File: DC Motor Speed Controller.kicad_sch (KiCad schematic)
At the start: 15 parts, among them J1 Screw_Terminal_01x02, J2 Screw_Terminal_01x02, Q1 TIP122, U1 NE555P

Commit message: Assigned Footprints to Components
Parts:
- C1, C2: footprint (none) -> Capacitor_THT:C_Disc_D4.7mm_W2.5mm_P5.00mm
- C3: footprint (none) -> Capacitor_THT:CP_Radial_D10.0mm_P5.00mm
- D4: footprint (none) -> LED_THT:LED_D5.0mm
- J1, J2: footprint (none) -> TerminalBlock:TerminalBlock_bornier-2_P5.08mm
- R1, R2, R3: footprint (none) -> Resistor_THT:R_Axial_DIN0204_L3.6mm_D1.6mm_P7.62mm_Horizontal
- RV1: footprint (none) -> Potentiometer_THT:Potentiometer_Alps_RK097_Single_Horizontal_Switch
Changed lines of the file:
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@@
 			)
 		)
-		(property "Footprint" ""
+		(property "Footprint" "Potentiometer_THT:Potentiometer_Alps_RK097_Single_Horizontal_Switch"
 			(at 90.17 100.33 0)
 			(effects
@@
 			)
 		)
-		(property "Footprint" ""
+		(property "Footprint" "LED_THT:LED_D5.0mm"
 			(at 72.39 113.03 0)
 			(effects
@@
 			)
 		)
-		(property "Footprint" ""
+		(property "Footprint" "Capacitor_THT:CP_Radial_D10.0mm_P5.00mm"
 			(at 63.1952 104.14 0)
 			(effects
@@
 			)
 		)
-		(property "Footprint" ""
+		(property "Footprint" "Resistor_THT:R_Axial_DIN0204_L3.6mm_D1.6mm_P7.62mm_Horizontal"
 			(at 171.45 91.948 90)
 			(effects
@@
 			)
 		)
-		(property "Footprint" ""
+		(property "Footprint" "Capacitor_THT:C_Disc_D4.7mm_W2.5mm_P5.00mm"
 			(at 91.1352 118.11 0)
 			(effects
@@
 			)
 		)
-		(property "Footprint" ""
+		(property "Footprint" "Capacitor_THT:C_Disc_D4.7mm_W2.5mm_P5.00mm"
 			(at 119.0752 118.11 0)
 			(effects
@@
 			)
 		)
-		(property "Footprint" ""
+		(property "Footprint" "Resistor_THT:R_Axial_DIN0204_L3.6mm_D1.6mm_P7.62mm_Horizontal"
 			(at 88.392 73.66 90)
 			(effects
@@
 			)
 		)
-		(property "Footprint" ""
+		(property "Footprint" "TerminalBlock:TerminalBlock_bornier-2_P5.08mm"
 			(at 210.82 74.93 0)
 			(effects
@@
 			)
 		)
-		(property "Footprint" ""
+		(property "Footprint" "Resistor_THT:R_Axial_DIN0204_L3.6mm_D1.6mm_P7.62mm_Horizontal"
 			(at 70.612 73.66 90)
 			(effects
@@
 			)
 		)
-		(property "Footprint" ""
+		(property "Footprint" "TerminalBlock:TerminalBlock_bornier-2_P5.08mm"
 			(at 46.99 97.79 0)
 			(effects

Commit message: Assigned the Error footprint
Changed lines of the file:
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@@
-	)
-	(symbol
-		(lib_id "Device:C")
-		(at 62.23 100.33 0)
-		(unit 1)
-		(exclude_from_sim no)
-		(in_bom yes)
-		(on_board yes)
-		(dnp no)
-		(property "Reference" "C3"
-			(at 66.04 99.0599 0)
-			(effects
-				(font
-					(size 1.27 1.27)
-				)
-				(justify left)
-			)
-		)
-		(property "Value" "1000uF"
-			(at 63.754 109.22 90)
-			(effects
-				(font
-					(size 1.27 1.27)
-				)
-				(justify left)
-			)
-		)
-		(property "Footprint" "Capacitor_THT:CP_Radial_D10.0mm_P5.00mm"
-			(at 63.1952 104.14 0)
-			(effects
-				(font
-					(size 1.27 1.27)
-				)
-				(hide yes)
-			)
-		)
-		(property "Datasheet" "~"
-			(at 62.23 100.33 0)
-			(effects
-				(font
-					(size 1.27 1.27)
-				)
-				(hide yes)
-			)
-		)
-		(property "Description" "Unpolarized capacitor"
-			(at 62.23 100.33 0)
-			(effects
-				(font
-					(size 1.27 1.27)
-				)
-				(hide yes)
-			)
-		)
-		(pin "2"
-		)
-		(pin "1"
-		)
-		(instances
-			(project "DC Motor Speed Controller"
-				(path "/f6006c76-6b8e-4b9c-acef-dbdcf88c8838"
-					(reference "C3")
-					(unit 1)
-				)
-			)
-		)
 	)
 	(symbol
@@
 					(unit 1)
 				)
+			)
+		)
+	)
+	(symbol
+		(lib_id "Device:C")
+		(at 62.23 100.33 0)
+		(unit 1)
+		(exclude_from_sim no)
+		(in_bom yes)
+		(on_board yes)
+		(dnp no)
+		(fields_autoplaced yes)
+		(property "Reference" "C3"
+			(at 66.04 99.0599 0)
+			(effects
+				(font
+					(size 1.27 1.27)
+				)
+				(justify left)
+			)
+		)
+		(property "Value" "1000uF"
+			(at 66.04 101.5999 0)
+			(effects
+				(font
+					(size 1.27 1.27)
+				)
+				(justify left)
+			)
+		)
+		(property "Footprint" "Capacitor_THT:CP_Radial_D10.0mm_P5.00mm"
+			(at 63.1952 104.14 0)
+			(effects
+				(font
+					(size 1.27 1.27)
+				)
+				(hide yes)
+			)
+		)
+		(property "Datasheet" "~"
+			(at 62.23 100.33 0)
+			(effects
+				(font
+					(size 1.27 1.27)
+				)
+				(hide yes)
+			)
+		)
+		(property "Description" "Unpolarized capacitor"
+			(at 62.23 100.33 0)
+			(effects
+				(font
+					(size 1.27 1.27)
+				)
+				(hide yes)
+			)
+		)
+		(pin "1"
+		)
+		(pin "2"
+		)
+		(instances
+			(project ""
+				(path "/f6006c76-6b8e-4b9c-acef-dbdcf88c8838"
+					(reference "C3")
+					(unit 1)
+				)

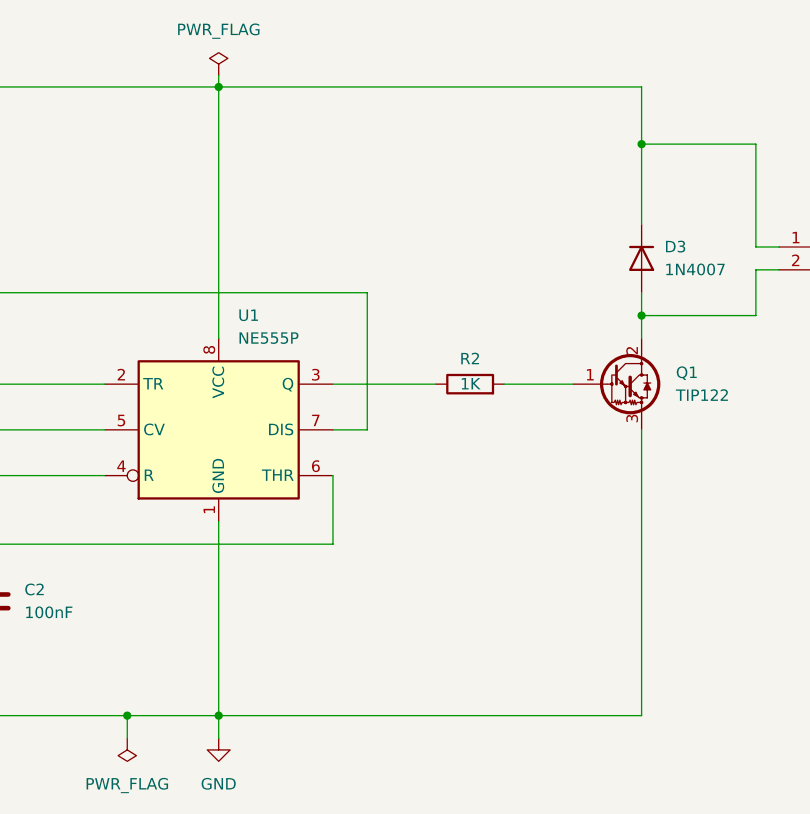
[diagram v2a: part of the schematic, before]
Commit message: Schematic without ERC error
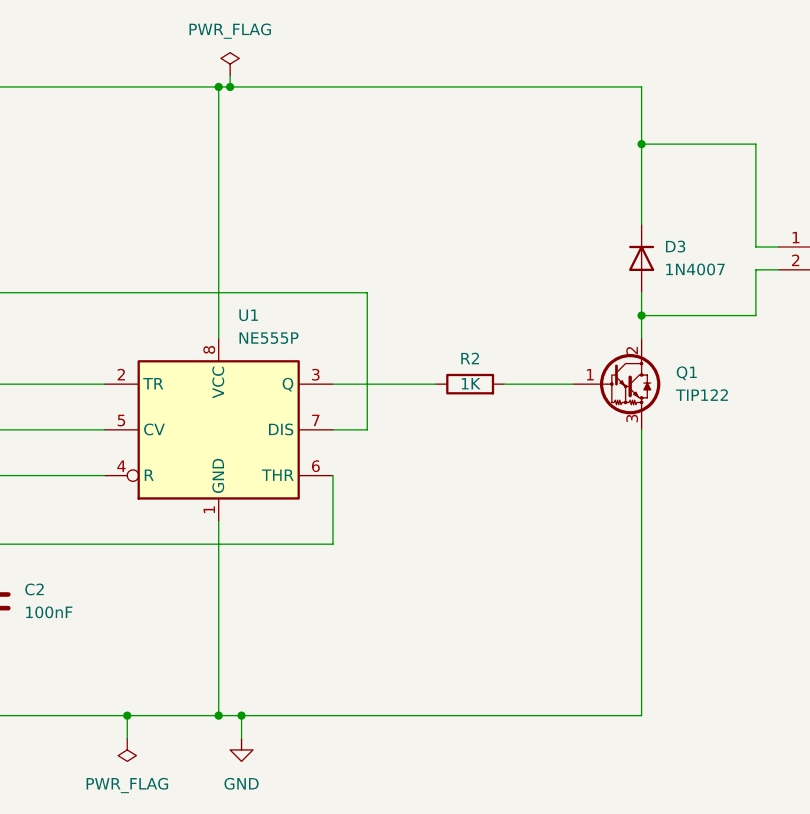
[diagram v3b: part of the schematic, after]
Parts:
- C3: footprint Capacitor_THT:CP_Radial_D10.0mm_P5.00mm -> Capacitor_THT:C_Radial_D8.0mm_H7.0mm_P3.50mm
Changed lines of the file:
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@@
+	)
+	(junction
+		(at 146.05 127)
+		(diameter 0)
+		(color 0 0 0 0)
 	)
 	(junction
@@
 	)
 	(junction
+		(at 144.78 57.15)
+		(diameter 0)
+		(color 0 0 0 0)
+	)
+	(junction
 		(at 97.79 82.55)
 		(diameter 0)
@@
 	(wire
 		(pts
-			(xy 190.5 57.15) (xy 143.51 57.15)
+			(xy 190.5 57.15) (xy 144.78 57.15)
 		)
 		(stroke
@@
 	(wire
 		(pts
-			(xy 143.51 127) (xy 143.51 129.54)
-		)
-		(stroke
-			(width 0)
-			(type default)
-		)
-	)
-	(wire
-		(pts
-			(xy 143.51 55.88) (xy 143.51 57.15)
-		)
-		(stroke
-			(width 0)
-			(type default)
-		)
-	)
-	(wire
-		(pts
 			(xy 62.23 96.52) (xy 62.23 57.15)
 		)
@@
 	(wire
 		(pts
+			(xy 144.78 57.15) (xy 143.51 57.15)
+		)
+		(stroke
+			(width 0)
+			(type default)
+		)
+	)
+	(wire
+		(pts
 			(xy 205.74 74.93) (xy 203.2 74.93)
 		)
@@
 	(wire
 		(pts
+			(xy 146.05 127) (xy 146.05 129.54)
+		)
+		(stroke
+			(width 0)
+			(type default)
+		)
+	)
+	(wire
+		(pts
 			(xy 97.79 82.55) (xy 97.79 85.09)
 		)
@@
 	(wire
 		(pts
-			(xy 190.5 127) (xy 143.51 127)
+			(xy 146.05 127) (xy 143.51 127)
+		)
+		(stroke
+			(width 0)
+			(type default)
+		)
+	)
+	(wire
+		(pts
+			(xy 190.5 127) (xy 146.05 127)
 		)
 		(stroke
@@
 		(pts
 			(xy 62.23 127) (xy 72.39 127)
+		)
+		(stroke
+			(width 0)
+			(type default)
+		)
+	)
+	(wire
+		(pts
+			(xy 144.78 55.88) (xy 144.78 57.15)
 		)
 		(stroke
@@
 	(symbol
 		(lib_id "power:PWR_FLAG")
-		(at 143.51 55.88 0)
+		(at 144.78 55.88 0)
 		(unit 1)
 		(exclude_from_sim no)
@@
 		(fields_autoplaced yes)
 		(property "Reference" "#FLG02"
-			(at 143.51 53.975 0)
+			(at 144.78 53.975 0)
 			(effects
 				(font
@@
 		)
 		(property "Value" "PWR_FLAG"
-			(at 143.51 50.8 0)
+			(at 144.78 50.8 0)
 			(effects
 				(font
@@
 		)
 		(property "Footprint" ""
-			(at 143.51 55.88 0)
+			(at 144.78 55.88 0)
 			(effects
 				(font
@@
 		)
 		(property "Datasheet" "~"
-			(at 143.51 55.88 0)
+			(at 144.78 55.88 0)
 			(effects
 				(font
@@
 		)
 		(property "Description" "Special symbol for telling ERC where power comes from"
-			(at 143.51 55.88 0)
+			(at 144.78 55.88 0)
 			(effects
 				(font
@@
 			)
 		)
-		(property "Footprint" "Capacitor_THT:CP_Radial_D10.0mm_P5.00mm"
+		(property "Footprint" "Capacitor_THT:C_Radial_D8.0mm_H7.0mm_P3.50mm"
 			(at 63.1952 104.14 0)
 			(effects
@@
 	(symbol
 		(lib_id "power:GND")
-		(at 143.51 129.54 0)
+		(at 146.05 129.54 0)
 		(unit 1)
 		(exclude_from_sim no)
@@
 		(fields_autoplaced yes)
 		(property "Reference" "#PWR01"
-			(at 143.51 135.89 0)
+			(at 146.05 135.89 0)
 			(effects
 				(font
@@
 		)
 		(property "Value" "GND"
-			(at 143.51 134.62 0)
+			(at 146.05 134.62 0)
 			(effects
 				(font
@@
 		)
 		(property "Footprint" ""
-			(at 143.51 129.54 0)
+			(at 146.05 129.54 0)
 			(effects
 				(font
@@
 		)
 		(property "Datasheet" ""
-			(at 143.51 129.54 0)
+			(at 146.05 129.54 0)
 			(effects
 				(font
@@
 		)
 		(property "Description" "Power symbol creates a global label with name \"GND\" , ground"
-			(at 143.51 129.54 0)
-			(effects
-				(font
+			(at 146.05 129.54 0)
+			(effects
+				(font

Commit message: Updated the Potentiometer Footprint
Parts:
- RV1: footprint Potentiometer_THT:Potentiometer_Alps_RK097_Single_Horizontal_Switch -> Potentiometer_THT:Potentiometer_Alps_RK163_Single_Horizontal
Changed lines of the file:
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@@
 			)
 		)
-		(property "Footprint" "Potentiometer_THT:Potentiometer_Alps_RK097_Single_Horizontal_Switch"
+		(property "Footprint" "Potentiometer_THT:Potentiometer_Alps_RK163_Single_Horizontal"
 			(at 90.17 100.33 0)
 			(effects
